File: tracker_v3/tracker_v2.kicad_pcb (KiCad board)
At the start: 2 copper layers, 72.5 x 22.1 mm, 37 parts, among them J1 USB_C_Receptacle_PowerOnly_6P, J2 P70-7000045, J3 P70-7000045, Q1 DMG9926UDM-7, U1 XIAO-ESP32-DIP, U2 LIS3DH, U3 DW01A, U4 INA226AIDGSR, U5 TP4056-42-ESOP8

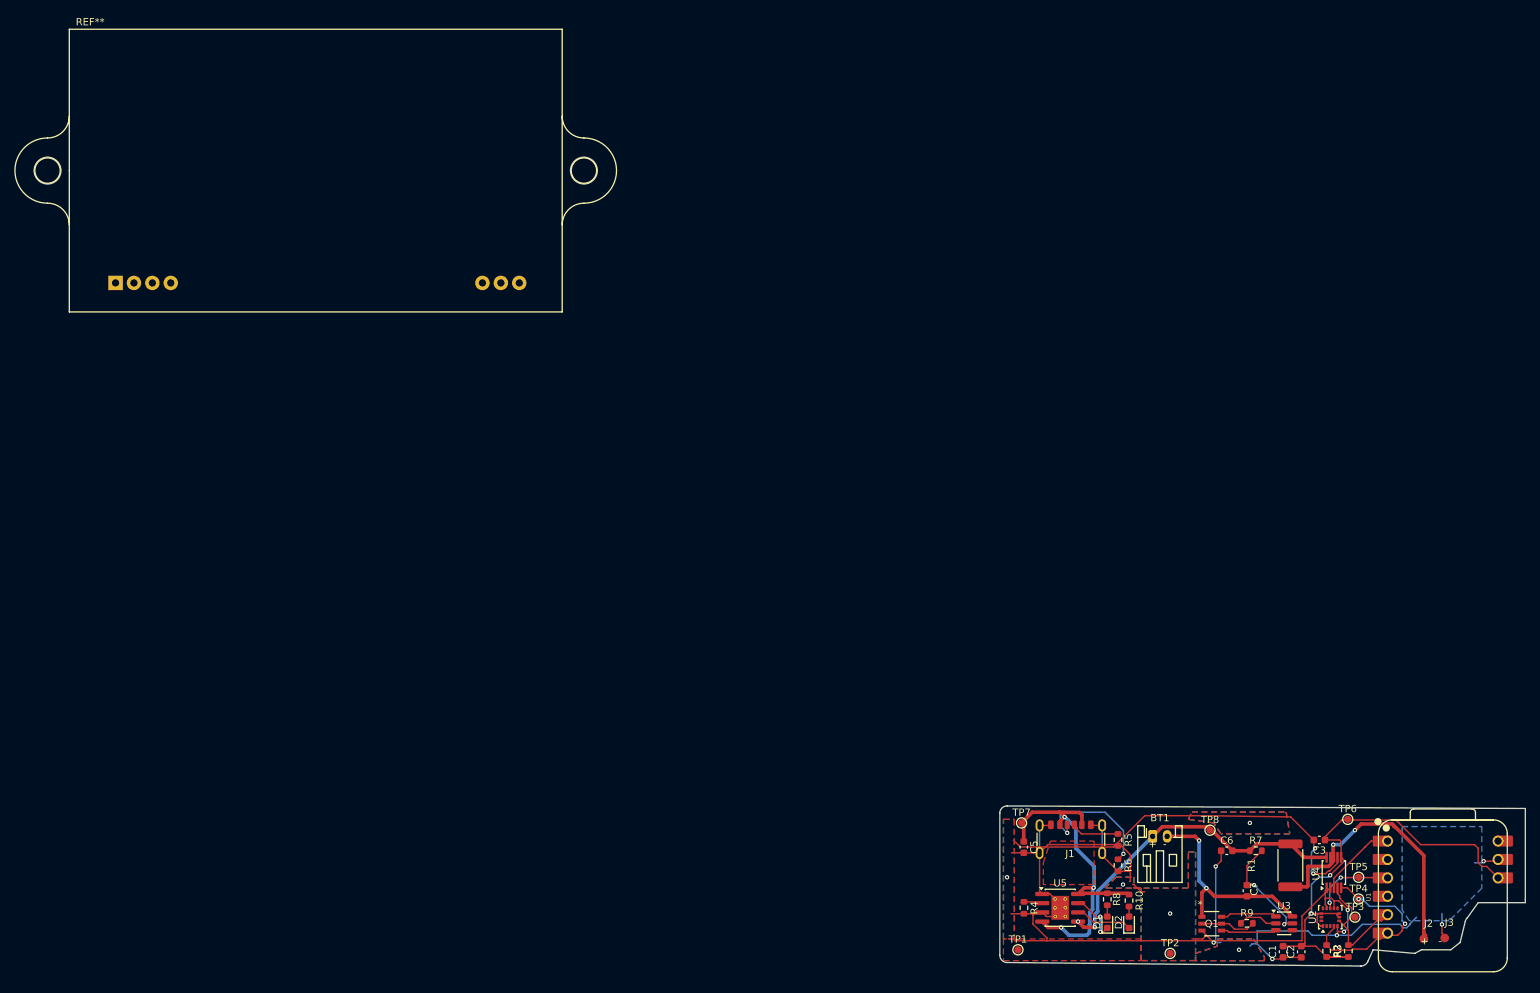
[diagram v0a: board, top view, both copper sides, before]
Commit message: added pogo pins to tracker_v3
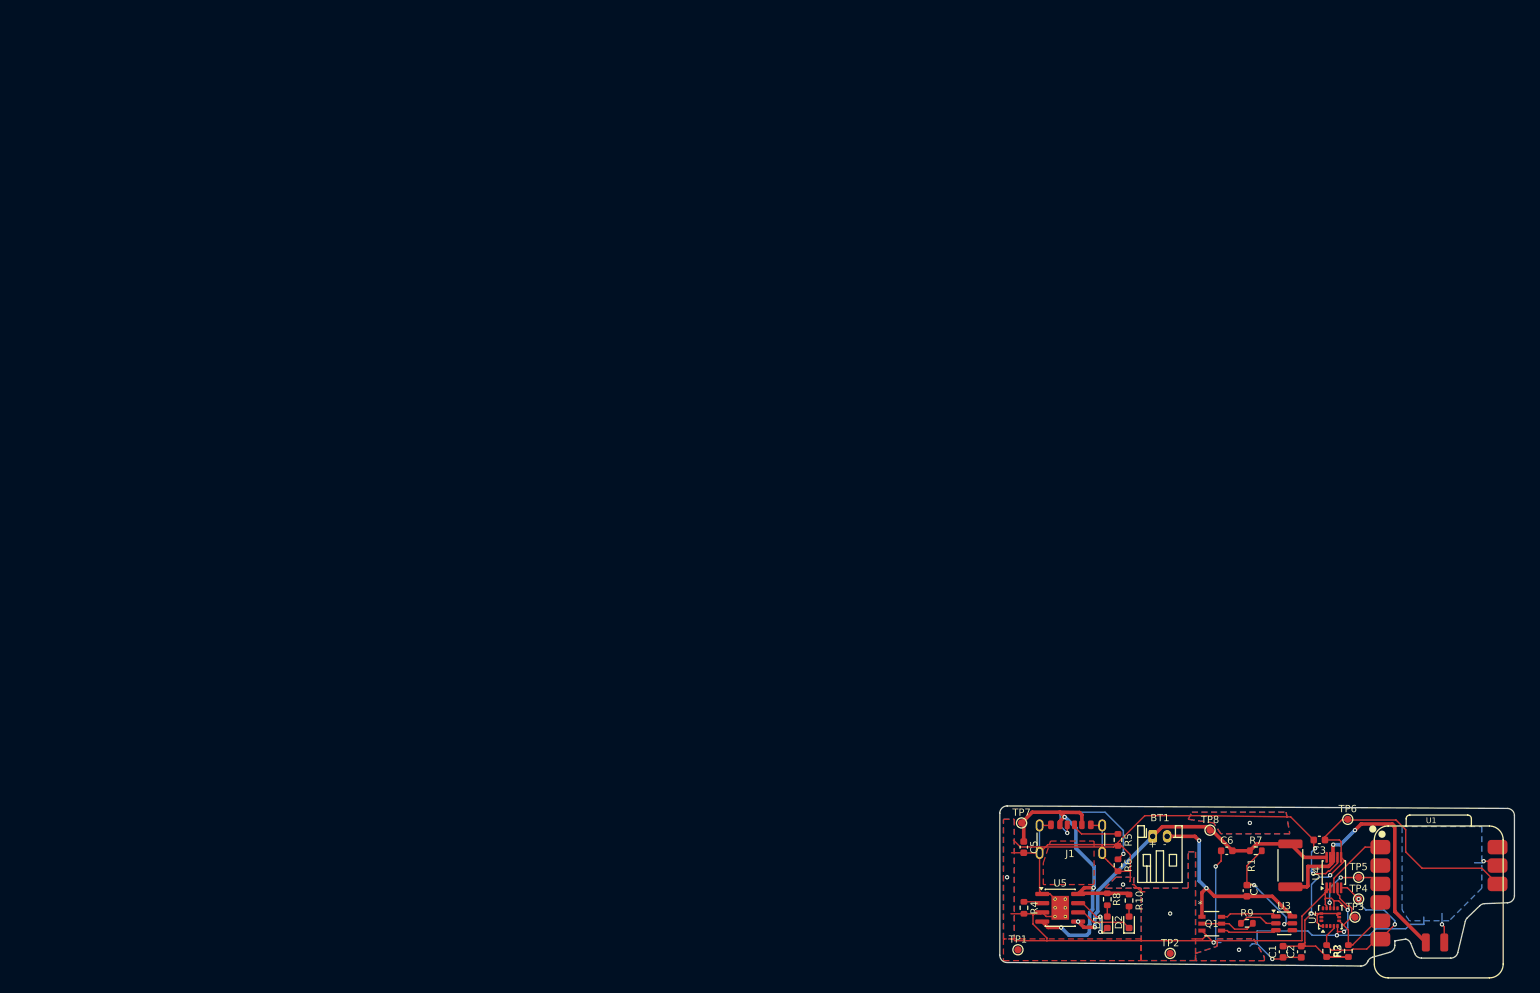
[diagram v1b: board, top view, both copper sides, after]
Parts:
- removed J2, J3: P70-7000045, P70_7000045:HARWIN_P70-7000045
- removed REF**: Reverb_BTDR-1H, Audio_Module:Reverb_BTDR-1H
- U1: value XIAO-ESP32-DIP -> XIAO-ESP32-C6-SMD; footprint Seeed_Studio_XIAO_Series:XIAO-ESP32-C6-DIP -> Seeed_Studio_XIAO_Series:XIAO-ESP32-C6-SMD
- moved U1 14.8 mm to (173.7, 96.0), turned to 0 degrees
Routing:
- net SCL: track 27.7 -> 24.3 mm
- net GND: track 233.5 -> 235.6 mm
- net Net-(U1-D0): track 10.9 -> 9.51 mm
- net SDA: track 17.6 -> 16.2 mm
- net /Shunt_Output: track 37.7 -> 38.7 mm
- net 3v3: track 69.8 -> 70.7 mm
- net Net-(U1-D2): track 11.6 -> 10.8 mm
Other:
- board size 72.5 x 22.1 mm -> 71 x 22.1 mm
